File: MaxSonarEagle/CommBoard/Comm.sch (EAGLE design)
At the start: 1 part

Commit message: schematic updates
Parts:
- added S1, S2: (no value), SparkFun-Switches:DIP-08-PTH
- added U$1, U$2, U$3, U$4, U$5, U$6, U$7, U$8: LV-MAXSONAR-EZ, Comm:LV-MAXSONAR-EZ
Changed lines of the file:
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@@
 <layer number="230" name="230bmp" color="7" fill="1" visible="yes" active="yes"/>
 <layer number="231" name="231bmp" color="7" fill="1" visible="yes" active="yes"/>
+<layer number="232" name="Eagle3D_PG2" color="7" fill="1" visible="no" active="no"/>
+<layer number="233" name="Eagle3D_PG3" color="7" fill="1" visible="no" active="no"/>
 <layer number="248" name="Housing" color="7" fill="1" visible="yes" active="yes"/>
 <layer number="249" name="Edge" color="7" fill="1" visible="yes" active="yes"/>
@@
 <parts>
 <part name="FRAME1" library="SparkFun-Aesthetics" deviceset="FRAME-LEDGER" device=""/>
+<part name="U$1" library="Comm" deviceset="LV-MAXSONAR-EZ" device=""/>
+<part name="U$2" library="Comm" deviceset="LV-MAXSONAR-EZ" device=""/>
+<part name="U$3" library="Comm" deviceset="LV-MAXSONAR-EZ" device=""/>
+<part name="U$4" library="Comm" deviceset="LV-MAXSONAR-EZ" device=""/>
+<part name="U$5" library="Comm" deviceset="LV-MAXSONAR-EZ" device=""/>
+<part name="U$6" library="Comm" deviceset="LV-MAXSONAR-EZ" device=""/>
+<part name="U$7" library="Comm" deviceset="LV-MAXSONAR-EZ" device=""/>
+<part name="U$8" library="Comm" deviceset="LV-MAXSONAR-EZ" device=""/>
+<part name="S1" library="SparkFun-Switches" deviceset="DIP-08" device="-PTH"/>
+<part name="S2" library="SparkFun-Switches" deviceset="DIP-08" device="-PTH"/>
 </parts>
 <sheets>
@@
 <instance part="FRAME1" gate="G$1" x="0" y="0"/>
 <instance part="FRAME1" gate="G$2" x="330.2" y="0"/>
+<instance part="U$1" gate="G$1" x="20.32" y="180.34"/>
+<instance part="U$2" gate="G$1" x="20.32" y="152.4"/>
+<instance part="U$3" gate="G$1" x="20.32" y="124.46"/>
+<instance part="U$4" gate="G$1" x="20.32" y="93.98"/>
+<instance part="U$5" gate="G$1" x="53.34" y="180.34"/>
+<instance part="U$6" gate="G$1" x="53.34" y="152.4"/>
+<instance part="U$7" gate="G$1" x="53.34" y="124.46"/>
+<instance part="U$8" gate="G$1" x="53.34" y="93.98"/>
+<instance part="S1" gate="A" x="147.32" y="185.42"/>
+<instance part="S2" gate="A" x="147.32" y="147.32"/>
 </instances>
 <busses>

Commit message: finalized board
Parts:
- removed S1: (no value), SparkFun-Switches:DIP-08-PTH
- added D1, D11, D13, D15, D3, D33, D37, D5, D7, D9: (no value), SparkFun-LED:LED0603
- added H1, H2, H3, H4: STAND-OFF, SparkFun-Hardware:STAND-OFF
- added J2: (no value), SparkFun-Connectors:CONN_06POLAR
- added Q1, Q10, Q19, Q2, Q21, Q22, Q23, Q24, Q25, Q26, Q27, Q3, Q4, Q5, Q6, Q7, Q8, Q9: 2N3904, SparkFun-DiscreteSemi:TRANS_NPN-MMBTA42
- added R1, R11, R13, R15, R3, R33, R5, R7, R9: 50, SparkFun-Resistors:RESISTOR0805
- added R10, R12, R14, R16, R17, R18, R2, R38, R4, R42, R44, R46, R48, R50, R52, R54, R6, R8: 1k, SparkFun-Resistors:RESISTOR0805
- added R19, R49: 10k, SparkFun-Resistors:RESISTOR0805
- added R37: 350, SparkFun-Resistors:RESISTOR0805
- added U1, U2: 74HC1G04, SparkFun-IC-Logic:74HC1G04
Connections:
- new net GND: J2.1, Q1.E, Q10.E, Q3.E, Q4.E, Q5.E, Q6.E, Q7.E, Q8.E, Q9.E, R19.1, R37.1, R49.1, U$1.BW, U$1.GND, U$2.BW, U$2.GND, U$3.BW, U$3.GND, U$4.BW, U$4.GND, U$5.BW, U$5.GND, U$6.BW, U$6.GND, U$7.BW, U$7.GND, U$8.BW, U$8.GND, U1G2.P$V-, U2G2.P$V-
- new net IO-UART-RX: J2.5, U1G1.Y
- new net IO-UART-TX: J2.4, U2G1.A
- new net IOTX: Q2.E, R19.2, R2.1, S2.1, U$1.RX
- new net N$1: D1.C, R1.2
- new net N$10: Q6.C, R9.1
- new net N$11: D11.C, R11.2
- new net N$12: Q7.C, R11.1
- new net N$13: D13.C, R13.2
- new net N$14: Q8.C, R13.1
- new net N$15: D15.C, R15.2
- new net N$16: Q9.C, R15.1
- new net N$17: Q2.B, R17.2
- new net N$18: Q10.C, R33.1
- new net N$2: Q1.C, R1.1
- new net N$20: Q10.B, R2.2
- new net N$22: Q9.B, R4.2
- new net N$24: Q8.B, R6.2
- new net N$26: Q7.B, R8.2
- new net N$28: Q6.B, R10.2
- new net N$3: D3.C, R3.2
- new net N$30: Q5.B, R12.2
- new net N$32: Q1.B, R14.2
- new net N$33: D33.C, R33.2
- new net N$34: Q3.B, R16.2
- new net N$37: D37.C, R37.2
- new net N$38: Q19.B, R38.2
- new net N$4: Q3.C, R3.1
- new net N$5: D5.C, R5.2
- new net N$6: Q4.C, R5.1
- new net N$61: Q21.B, R42.2
- new net N$63: Q4.B, R18.2
- new net N$65: Q22.B, R44.2
- new net N$68: Q23.B, R46.2
- new net N$7: D7.C, R7.2
- new net N$71: Q24.B, R48.2
- new net N$74: Q25.B, R50.2
- new net N$77: Q26.B, R52.2
- new net N$8: Q5.C, R7.1
- new net N$80: Q27.B, R54.2
- new net N$9: D9.C, R9.2
- new net RS232-RX: Q19.E, Q21.E, Q22.E, Q23.E, Q24.E, Q25.E, Q26.E, Q27.E, R49.2, U1G1.A
- new net RS232-TX: R17.1, U2G1.Y
- new net TX1: R14.1, R38.1, S2.16, S2.2, U$1.TX, U$2.RX
- new net TX2: R16.1, R42.1, S2.15, S2.3, U$2.TX, U$3.RX
- new net TX3: R18.1, R44.1, S2.14, S2.4, U$3.TX, U$4.RX
- new net TX4: R12.1, R46.1, S2.13, S2.5, U$4.TX, U$5.RX
- new net TX5: R10.1, R48.1, S2.12, S2.6, U$5.TX, U$6.RX
- new net TX6: R50.1, R8.1, S2.11, S2.7, U$6.TX, U$7.RX
- new net TX7: R52.1, R6.1, S2.10, S2.8, U$7.TX, U$8.RX
- new net TX8: R4.1, R54.1, S2.9, U$8.TX
- new net VIN: D1.A, D11.A, D13.A, D15.A, D3.A, D33.A, D37.A, D5.A, D7.A, D9.A, J2.3, Q19.C, Q2.C, Q21.C, Q22.C, Q23.C, Q24.C, Q25.C, Q26.C, Q27.C, U$1.+5, U$2.+5, U$3.+5, U$4.+5, U$5.+5, U$6.+5, U$7.+5, U$8.+5, U1G2.P$V+, U2G2.P$V+
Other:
- note added: "IO"
- note added: "Input TX Isolation"
- note added: "LEDs"
- note added: "RS232 Non-Inverting Bus"
- note added: "RS232 to UART Conversion"
- note added: "Sonar Connections"
- note added: "Standoffs"
- note added: "TX Bridge"
- note added: "This board provides an interface with up to 8 maxbotix sonar sensors. Each sensor has: 1. An bridge switch to enable when not in use 2. A status LED showing line communication The sonar system will provide a single data measurement from each sonar per input command from the IOTX line"
- note removed: "This board provides an interface with up to 8 maxbotix sonar sensors. Each sensor has: 1. An enable switch 2. An uart/rs232 select switch 3. A status LED showing line communication The sonar system will provide a single data measurement from each sonar per input command from the IOTX line"
- moved on the sheet: S2

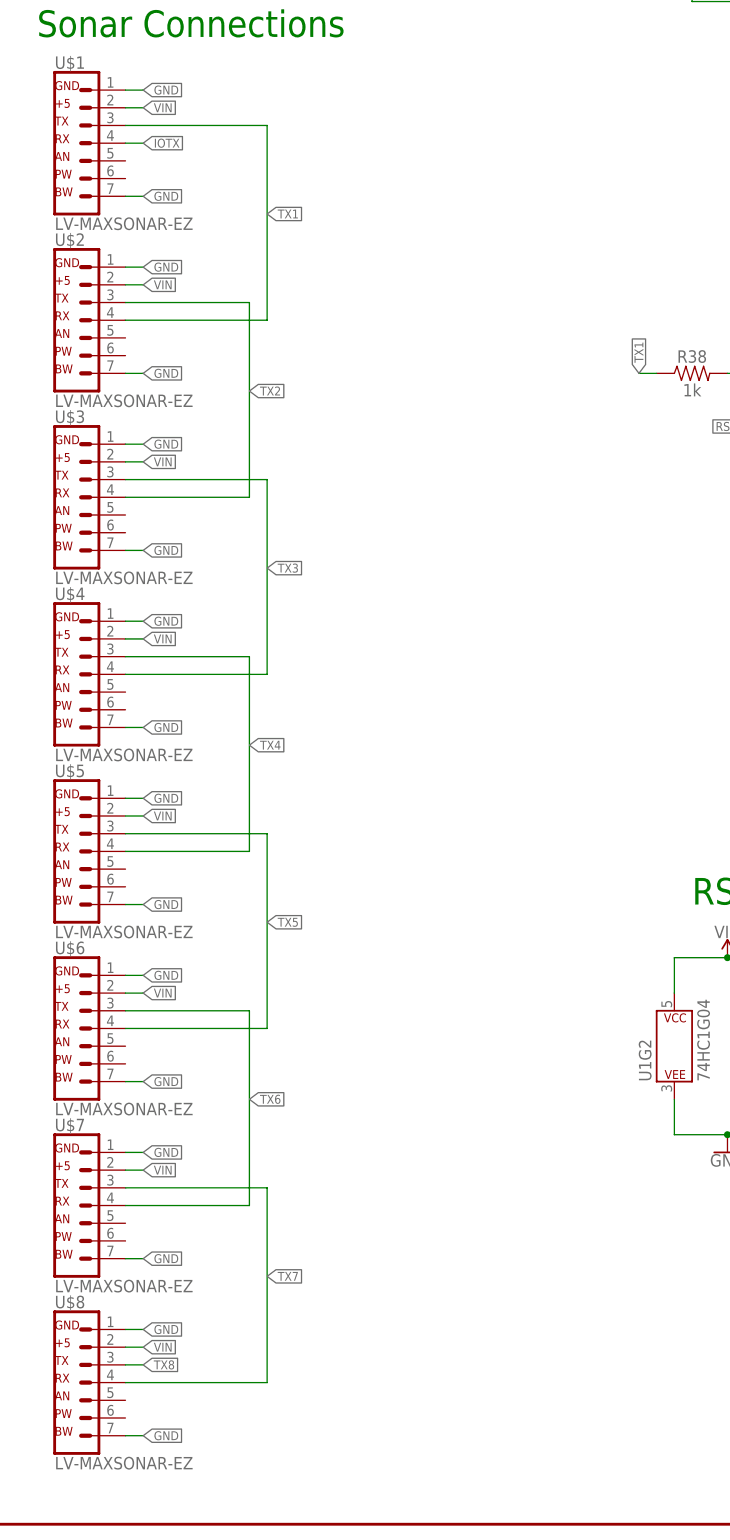
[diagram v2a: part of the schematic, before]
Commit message: added pulldown resistors to sonar rx lines
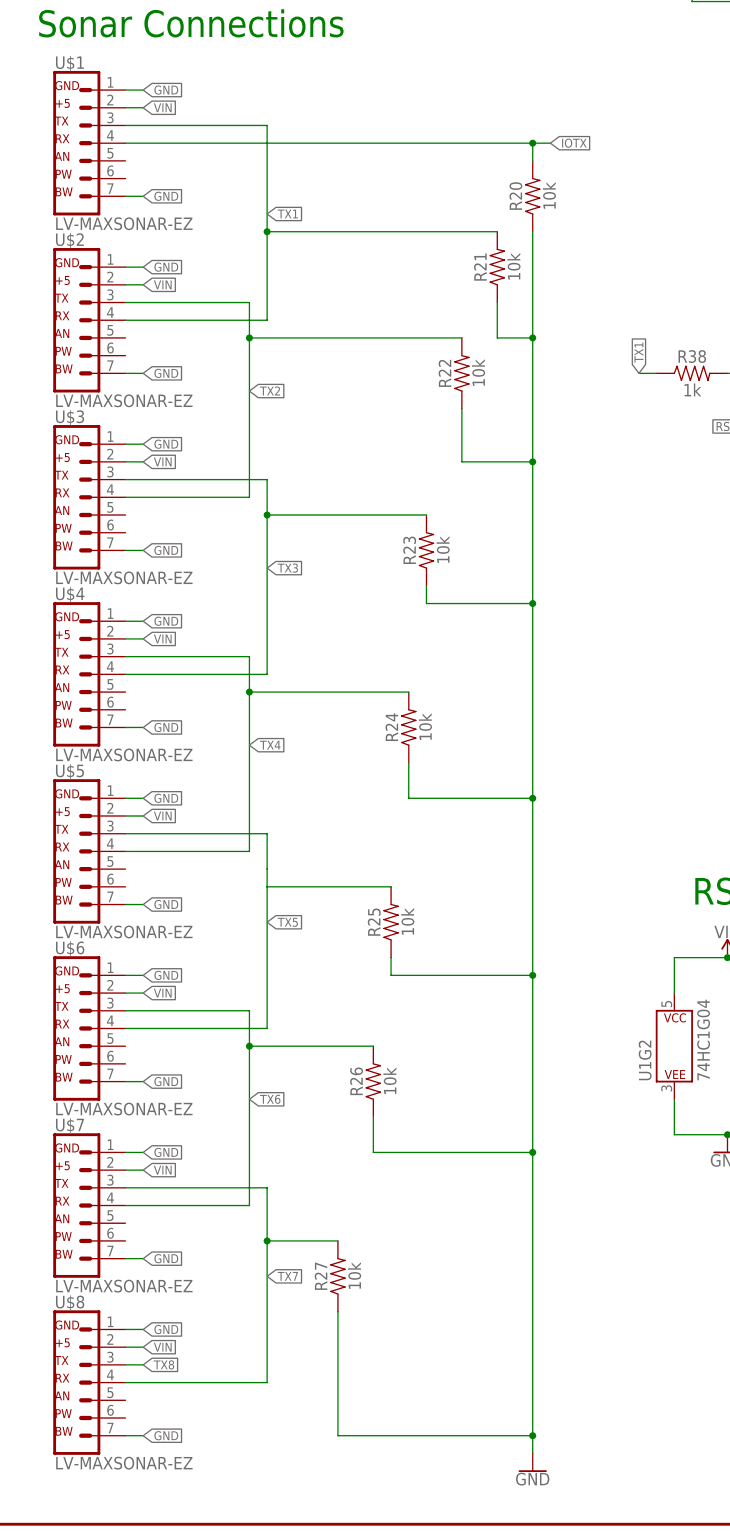
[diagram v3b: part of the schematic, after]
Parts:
- added R20, R21, R22, R23, R24, R25, R26, R27: 10k, SparkFun-Resistors:RESISTOR0805
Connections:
- net GND: now also R20.1, R21.1, R22.1, R23.1, R24.1, R25.1, R26.1, R27.1
- net IOTX: now also R20.2
- net TX1: now also R21.2
- net TX2: now also R22.2
- net TX3: now also R23.2
- net TX4: now also R24.2
- net TX5: now also R25.2
- net TX6: now also R26.2
- net TX7: now also R27.2
